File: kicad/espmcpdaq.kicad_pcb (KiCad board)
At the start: 2 copper layers, 165.1 x 148.6 mm, 32 parts, among them J1 Conn_01x02, J2 Conn_01x15_Female, J3 Conn_01x15_Female

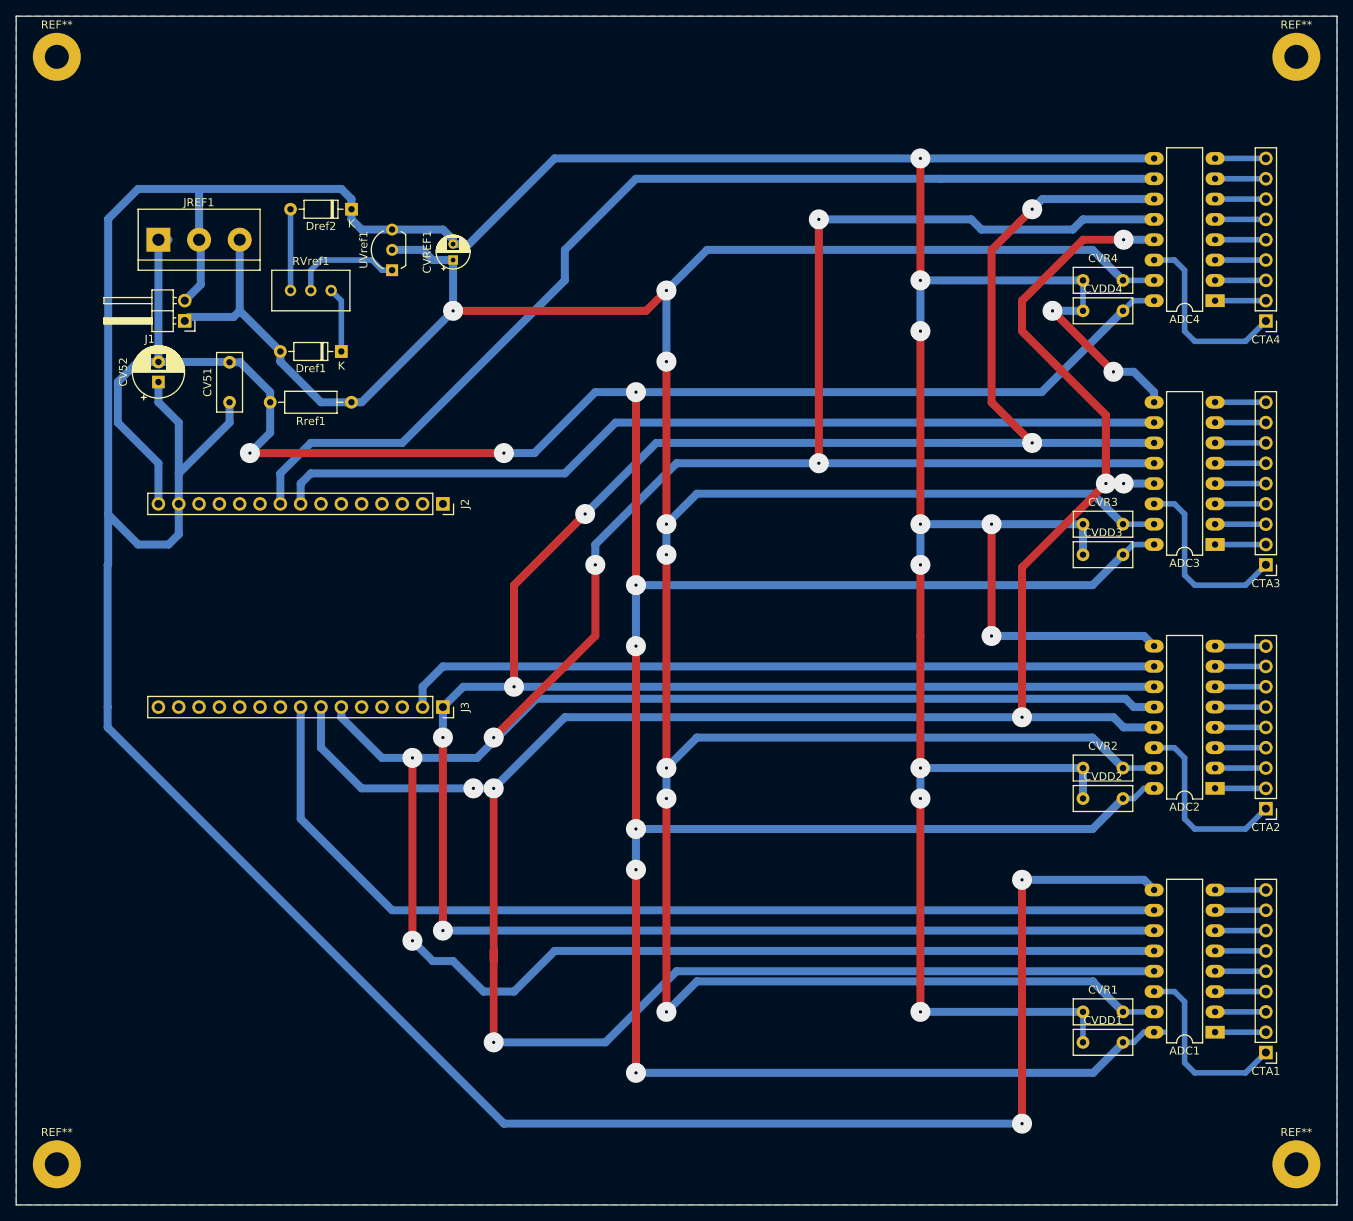
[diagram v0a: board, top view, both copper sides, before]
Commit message: Corrected hte ERC problems.
The issues kind of make sense. Since the same MISO and MOSI are used for every ADC, the system complains about connecting different outputs together. This not an issue because each ADC has different chip select wire. There were several warnings about unspecified pins connected to some other pins. I just asked KiCAD to ignore this

I still need to think about power supply for the board. The anemometers will use 24V and I could reduce this to 5V using a 78-5 or LM317 but they will run hot due to the large voltage drop. Another thing I should think about is how adding a button to select voltage source: USB or power supply. I think I will rearrange everything and add this feature.
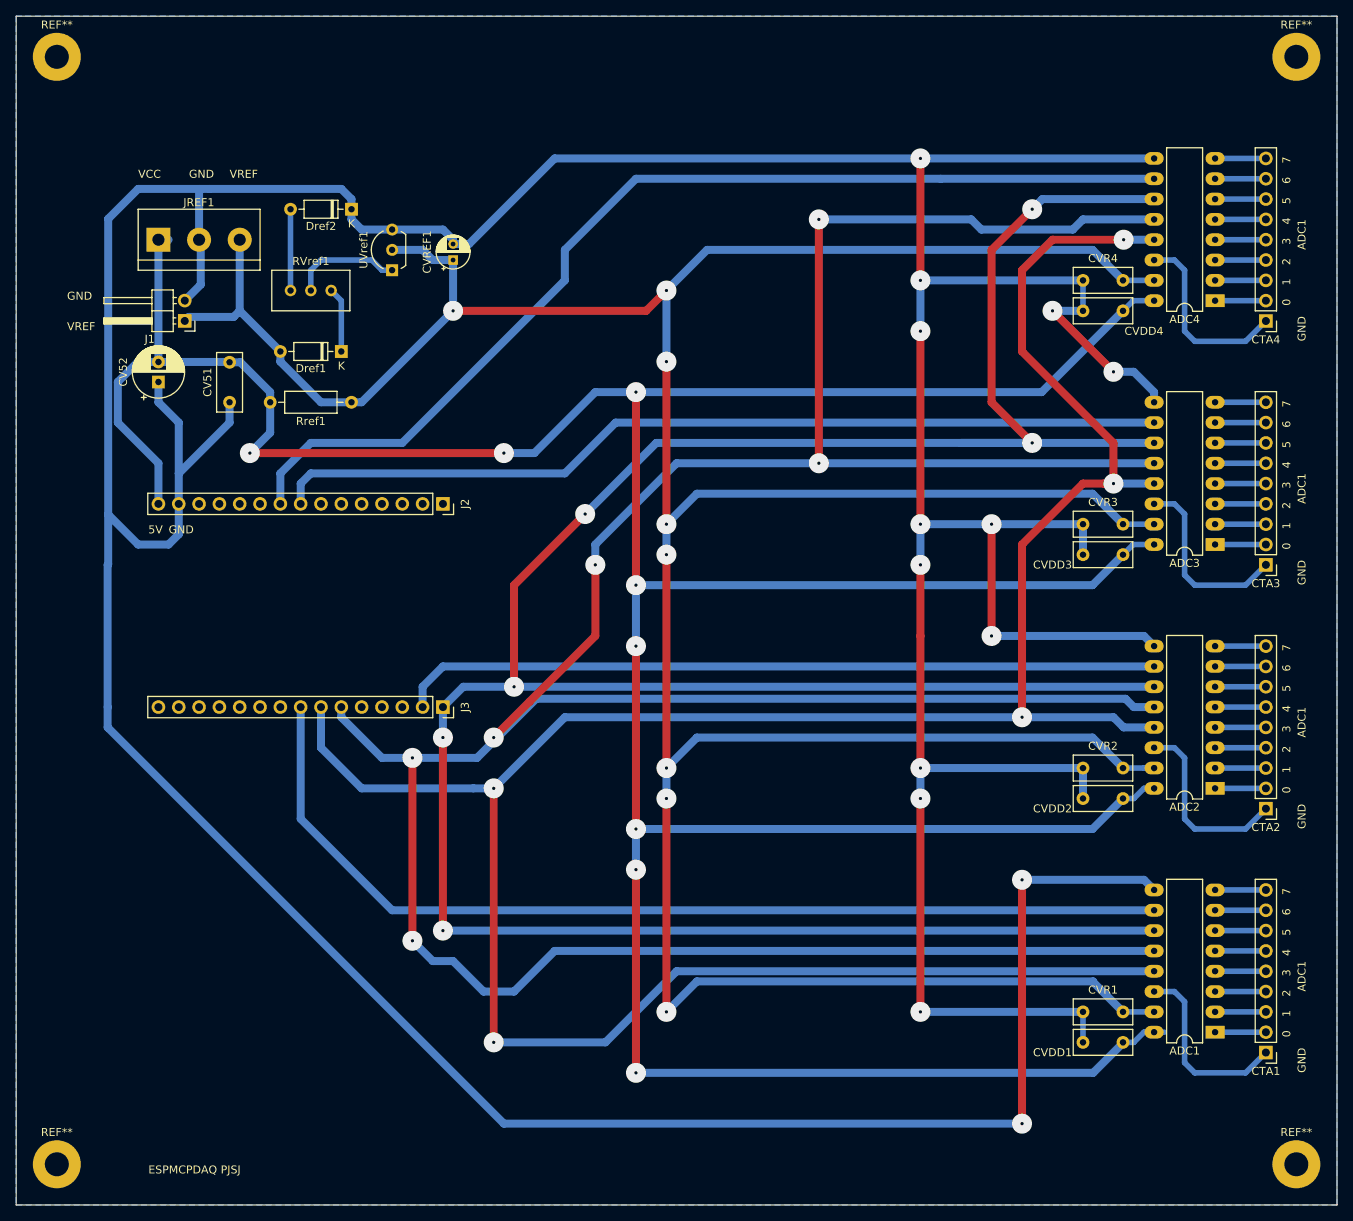
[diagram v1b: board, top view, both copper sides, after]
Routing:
- net /CLK: track 323.0 -> 324.3 mm, vias 7 -> 5
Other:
- board text added: "0"
- board text added: "1"
- board text added: "2"
- board text added: "3"
- board text added: "4"
- board text added: "5"
- board text added: "5V"
- board text added: "6"
- board text added: "7"
- board text added: "ADC1"
- board text added: "ESPMCPDAQ PJSJ"
- board text added: "GND"
- board text added: "VCC"
- board text added: "VREF"

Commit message: Added the possibility of choosing 5V input.
The 5V input can come from either a terminal or the esp board USB.

I've been thinking and I believe I should make the daq part independent
of the board. Therefore I should deal only with SPI lines and input voltage.
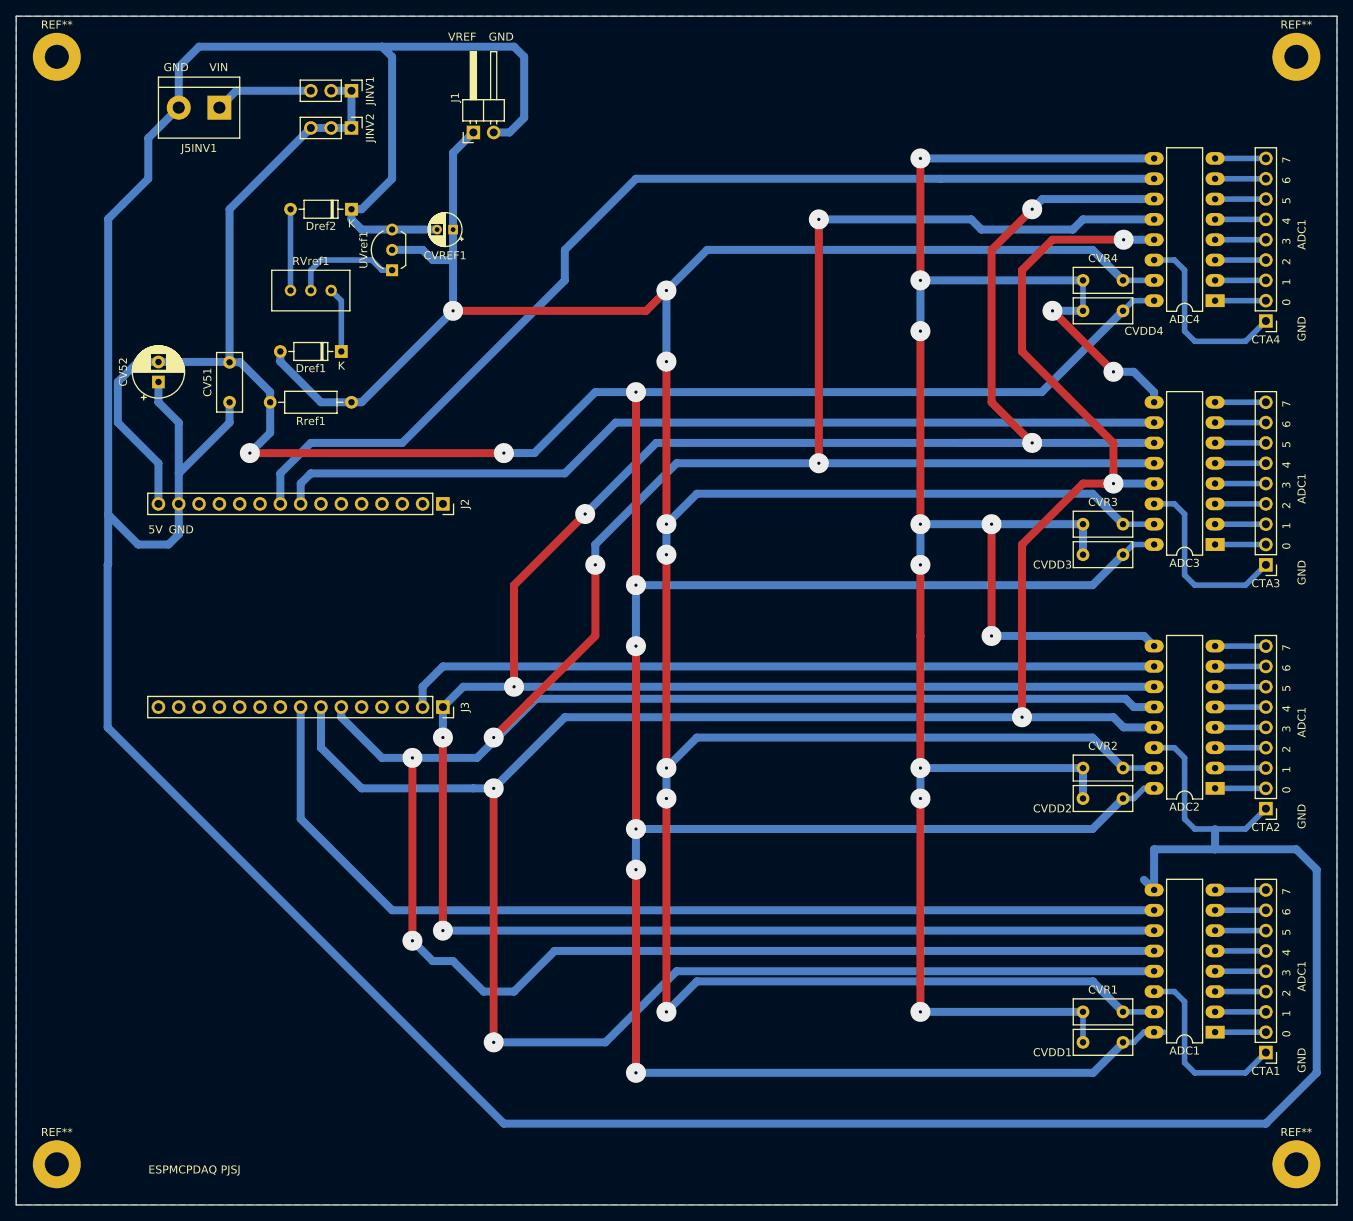
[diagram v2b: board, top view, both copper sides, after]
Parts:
- removed JREF1: Conn_01x03, TerminalBlock:TerminalBlock_bornier-3_P5.08mm
- added J5INV1: Conn_01x02, TerminalBlock:TerminalBlock_bornier-2_P5.08mm, F.Cu at (45.7, 25.4)
- added JINV1: Conn_01x03, Connector_PinHeader_2.54mm:PinHeader_1x03_P2.54mm_Vertical, F.Cu at (62.2, 23.3)
- added JINV2: Conn_01x03, Connector_PinHeader_2.54mm:PinHeader_1x03_P2.54mm_Vertical, F.Cu at (62.2, 27.9)
- moved J1 43.1 mm to (77.5, 28.5), turned to 90 degrees
- moved CVREF1 3.81 mm to (74.9, 40.6), turned to 180 degrees
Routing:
- net GND: track 799.5 -> 836.3 mm, vias 14 -> 12
- net /VDD: track 472.7 -> 501.4 mm
- net /5INV: track 0.00 -> 12.3 mm
- net /Vref: track 442.6 -> 436.1 mm
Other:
- board text added: "VIN"
- board text removed: "VCC"

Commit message: Just added a little text
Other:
- board text added: "CLK"
- board text added: "CS1"
- board text added: "CS2"
- board text added: "CS3"
- board text added: "CS4"
- board text added: "LM336-2.5V"
- board text added: "MISO"
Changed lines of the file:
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@@
 		(tags "CP Radial series Radial pin pitch 2.00mm  diameter 4mm Electrolytic Capacitor")
 		(property "Reference" "CVREF1"
-			(at 1 -3.25 360)
+			(at 1 -3.25 0)
 			(layer "F.SilkS")
 			(effects
@@
 		)
 		(property "Value" "1u"
-			(at 1 3.25 360)
+			(at 1 3.25 0)
 			(layer "F.Fab")
 			(effects
@@
 		)
 		(property "Footprint" "Capacitor_THT:CP_Radial_D4.0mm_P2.00mm"
-			(at 0 0 360)
+			(at 0 0 0)
 			(layer "F.Fab")
 			(hide yes)
@@
 		)
 		(property "Datasheet" ""
-			(at 0 0 360)
+			(at 0 0 0)
 			(layer "F.Fab")
 			(hide yes)
@@
 		)
 		(property "Description" ""
-			(at 0 0 360)
+			(at 0 0 0)
 			(layer "F.Fab")
 			(hide yes)
@@
 		)
 		(fp_text user "${REFERENCE}"
-			(at 1 0 360)
+			(at 1 0 0)
 			(layer "F.Fab")
 			(effects
@@
 		)
 		(fp_text user "${REFERENCE}"
-			(at 0 2.54 360)
+			(at 0 2.54 0)
 			(layer "F.Fab")
 			(effects
@@
 		)
 		(fp_text user "${REFERENCE}"
-			(at 0 2.54 360)
+			(at 0 2.54 0)
 			(layer "F.Fab")
 			(effects
@@
 		)
 		(fp_text user "${REFERENCE}"
-			(at 2.77 1.27 360)
+			(at 2.77 1.27 0)
 			(layer "F.Fab")
 			(effects
@@
 		(tags "terminal block bornier2")
 		(property "Reference" "J5INV1"
-			(at 2.54 -5.08 360)
+			(at 2.54 -5.08 0)
 			(layer "F.SilkS")
 			(effects
@@
 		)
 		(property "Value" "Conn_01x02"
-			(at 2.54 5.08 360)
+			(at 2.54 5.08 0)
 			(layer "F.Fab")
 			(effects
@@
 		)
 		(fp_text user "${REFERENCE}"
-			(at 2.54 0 360)
+			(at 2.54 0 0)
 			(layer "F.Fab")
 			(effects
@@
 		)
 	)
+	(gr_text "VIN"
+		(at 49.53 26.67 0)
+		(layer "F.SilkS")
+		(effects
+			(font
+				(size 1 1)
+				(thickness 0.15)
+			)
+			(justify left bottom)
+		)
+	)
 	(gr_text "4"
 		(at 179.705 131.445 90)
@@
 		)
 	)
+	(gr_text "CS3"
+		(at 56.515 73.025 90)
+		(layer "F.SilkS")
+		(effects
+			(font
+				(size 1 1)
+				(thickness 0.15)
+			)
+			(justify left bottom)
+		)
+	)
 	(gr_text "ADC1\n"
 		(at 181.61 43.18 90)
@@
 	)
 	(gr_text "GND"
+		(at 34.29 26.67 0)
+		(layer "F.SilkS")
+		(effects
+			(font
+				(size 1 1)
+				(thickness 0.15)
+			)
+			(justify left bottom)
+		)
+	)
+	(gr_text "GND"
 		(at 181.61 54.61 90)
 		(layer "F.SilkS")
@@
 		)
 	)
+	(gr_text "MISO"
+		(at 61.595 106.045 90)
+		(layer "F.SilkS")
+		(effects
+			(font
+				(size 1 1)
+				(thickness 0.15)
+			)
+			(justify left bottom)
+		)
+	)
+	(gr_text "CS2"
+		(at 71.755 105.41 90)
+		(layer "F.SilkS")
+		(effects
+			(font
+				(size 1 1)
+				(thickness 0.15)
+			)
+			(justify left bottom)
+		)
+	)
 	(gr_text "ADC1\n"
 		(at 181.61 74.93 90)
@@
 		)
 	)
+	(gr_text "CLK"
+		(at 59.055 105.41 90)
+		(layer "F.SilkS")
+		(effects
+			(font
+				(size 1 1)
+				(thickness 0.15)
+			)
+			(justify left bottom)
+		)
+	)
 	(gr_text "GND"
-		(at 39.37 78.74 0)
+		(at 41.275 72.39 90)
 		(layer "F.SilkS")
 		(effects
@@
 		)
 	)
+	(gr_text "CS1"
+		(at 56.515 105.41 90)
+		(layer "F.SilkS")
+		(effects
+			(font
+				(size 1 1)
+				(thickness 0.15)
+			)
+			(justify left bottom)
+		)
+	)
+	(gr_text "LM336-2.5V"
+		(at 70.485 47.625 90)
+		(layer "F.SilkS")
+		(effects
+			(font
+				(size 1 1)
+				(thickness 0.15)
+			)
+			(justify left bottom)
+		)
+	)
 	(gr_text "6"
 		(at 179.705 34.925 90)
@@
 		)
 	)
+	(gr_text "VREF"
+		(at 71.12 29.21 0)
+		(layer "F.SilkS")
+		(effects
+			(font
+				(size 1 1)
+				(thickness 0.15)
+			)
+			(justify left bottom)
+		)
+	)
 	(gr_text "4"
 		(at 179.705 100.965 90)
@@
 	)
 	(gr_text "5V"
-		(at 36.83 78.74 0)
+		(at 38.735 72.39 90)
+		(layer "F.SilkS")
+		(effects
+			(font
+				(size 1 1)
+				(thickness 0.15)
+			)
+			(justify left bottom)
+		)
+	)
+	(gr_text "CS4"
+		(at 53.975 73.025 90)
 		(layer "F.SilkS")
 		(effects
@@
 		(layer "F.SilkS")
 		(effects
+			(font
+				(size 1 1)
+				(thickness 0.15)
+			)
+			(justify left bottom)
+		)
+	)
+	(gr_text "GND"
+		(at 81.28 30.48 0)
+		(layer "F.SilkS")
+		(effects
